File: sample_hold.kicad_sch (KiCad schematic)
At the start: 47 parts, among them K21 G6K-2FY, 5V, Q21 AO3400A, Q22 AO3401A, Q23 AO3400A, Q24 AO3400A, Q25 AO3400A, Q26 AO3400A, Q27 AO3400A, Q28 BSS139, Q29 BSS139, U21 OPA828DGN, U22 OPA2197D, U23 TLV9352D

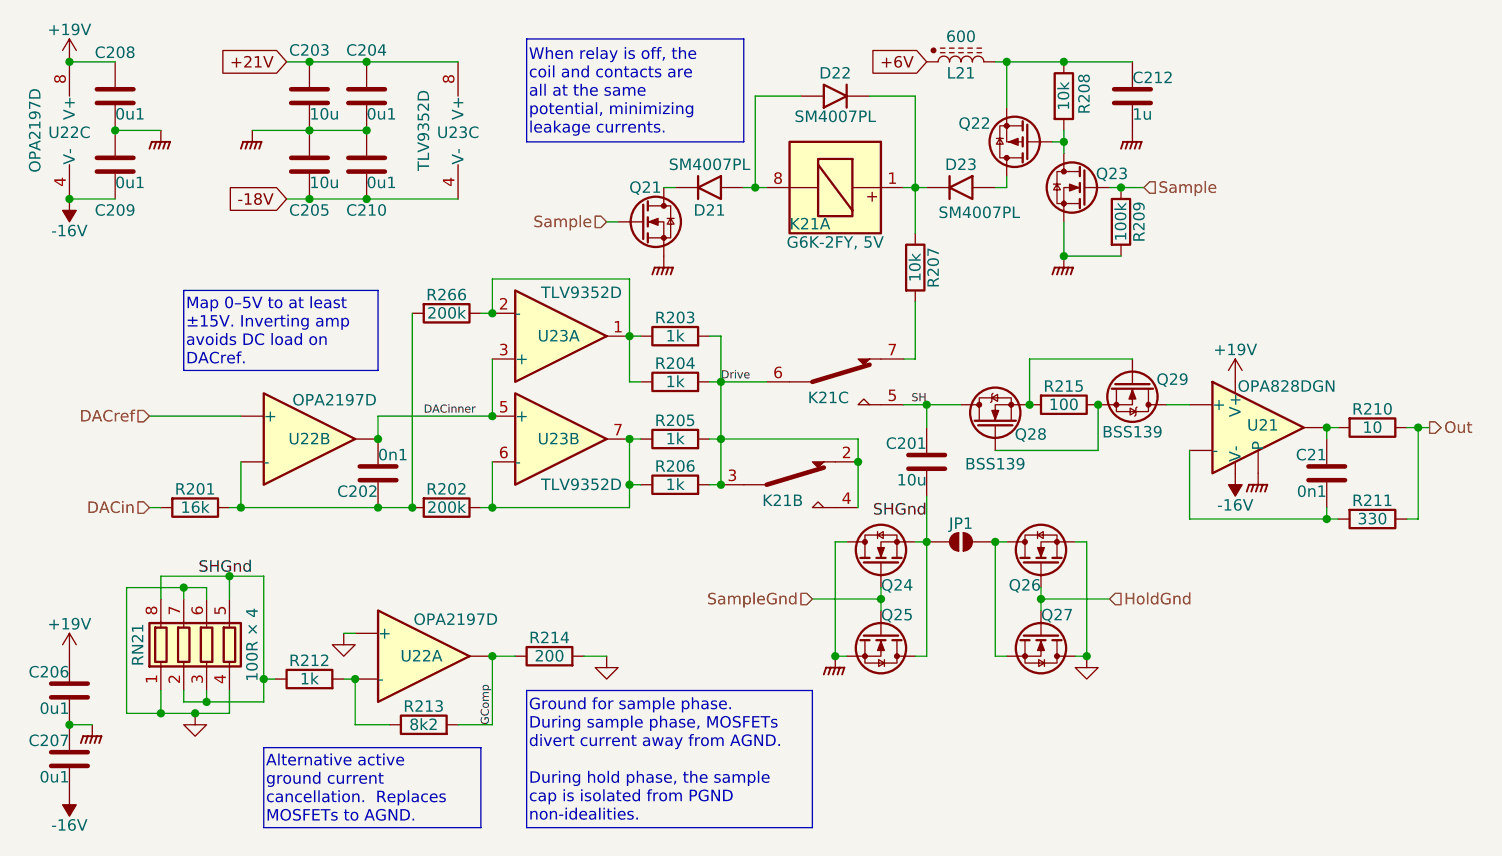
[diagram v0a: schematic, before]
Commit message: Nearly all routed.  Repinning FDA resistors.
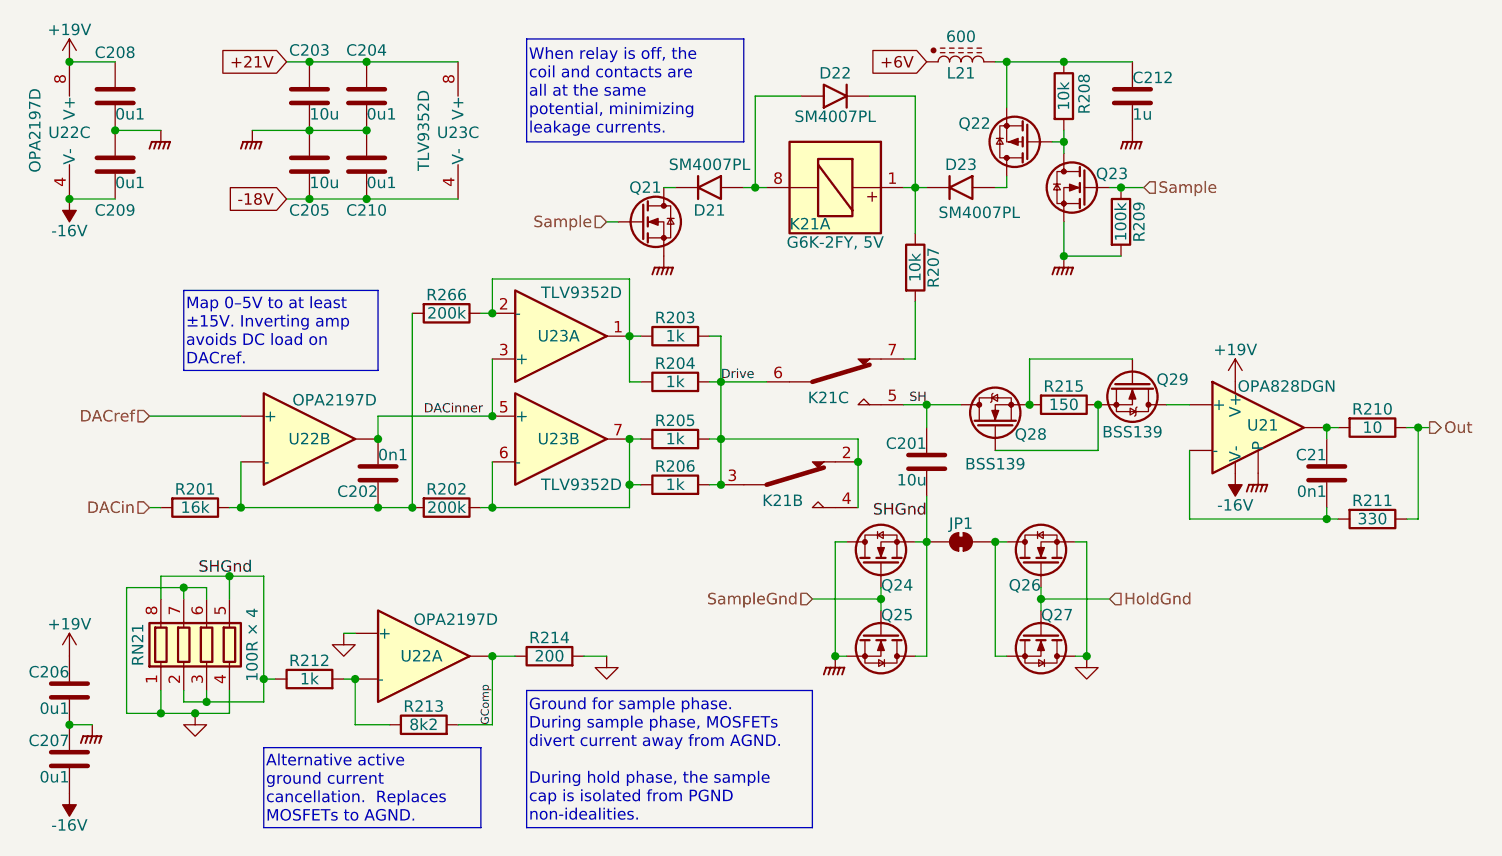
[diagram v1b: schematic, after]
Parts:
- C202, C21: footprint Capacitor_SMD:C_0402_1005Metric -> Capacitor_SMD:C_0603_1608Metric; LCSC C1546 -> (none)
- JP1: footprint Parts:JumperOpen -> Parts:JumperClosed; symbol Jumper:SolderJumper_2_Open -> Jumper:SolderJumper_2_Bridged
- R215: value 100 -> 150; LCSC (none) -> C25076
- U21: footprint Parts:OPA828DGN_guard -> Parts:OPA828DGN
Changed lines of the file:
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@@
 		(effects
 			(font
-				(size 0.889 0.889)
+				(size 1.016 1.016)
 			)
 			(justify left bottom)
@@
 			(font
 				(size 1.27 1.27)
+				(thickness 0.1588)
 			)
 			(justify right bottom)
@@
 		(effects
 			(font
-				(size 0.889 0.889)
+				(size 1.016 1.016)
 			)
 			(justify left bottom)
@@
 		(effects
 			(font
-				(size 0.889 0.889)
+				(size 1.016 1.016)
 			)
 			(justify right bottom)
@@
 			)
 		)
-		(property "Footprint" "Capacitor_SMD:C_0402_1005Metric"
+		(property "Footprint" "Capacitor_SMD:C_0603_1608Metric"
 			(at 106.3752 77.47 0)
 			(effects
@@
 			)
 		)
-		(property "LCSC" "C1546"
+		(property "LCSC" ""
 			(at 105.41 73.66 0)
 			(effects
@@
 			)
 		)
-		(property "Value" "100"
+		(property "Value" "150"
 			(at 181.61 66.04 90)
 			(effects
@@
 			)
 		)
-		(property "LCSC" ""
+		(property "LCSC" "C25076"
 			(at 181.61 66.04 90)
 			(effects
@@
 	)
 	(symbol
-		(lib_id "Jumper:SolderJumper_2_Open")
+		(lib_id "Jumper:SolderJumper_2_Bridged")
 		(at 170.18 81.28 0)
 		(unit 1)
@@
 			)
 		)
-		(property "Footprint" "Parts:JumperOpen"
+		(property "Footprint" "Parts:JumperClosed"
 			(at 170.18 81.28 0)
 			(effects
@@
 			)
 		)
-		(property "Description" "Solder Jumper, 2-pole, open"
+		(property "Description" "Solder Jumper, 2-pole, closed/bridged"
 			(at 170.18 81.28 0)
 			(effects
@@
 			)
 		)
-		(property "Footprint" "Parts:OPA828DGN_guard"
+		(property "Footprint" "Parts:OPA828DGN"
 			(at 200.66 73.66 0)
 			(effects
@@
 			)
 		)
-		(property "Footprint" "Capacitor_SMD:C_0402_1005Metric"
+		(property "Footprint" "Capacitor_SMD:C_0603_1608Metric"
 			(at 211.7852 77.47 0)
 			(effects
@@
 			)
 		)
-		(property "LCSC" "C1546"
+		(property "LCSC" ""
 			(at 210.82 73.66 0)
 			(effects

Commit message: DRC update.  Repin ADC.  De-crack the S/H ground.
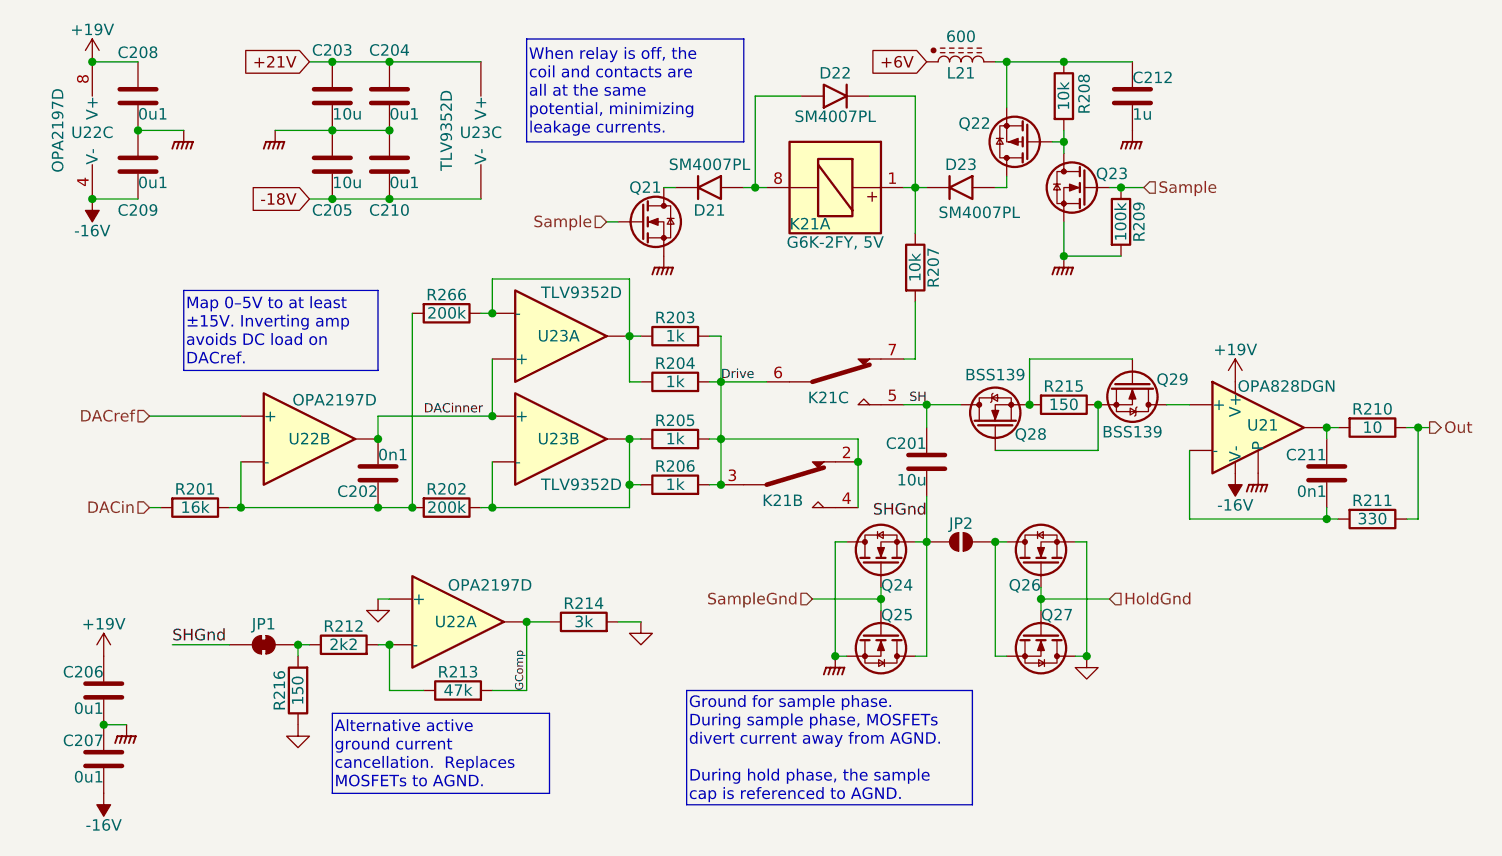
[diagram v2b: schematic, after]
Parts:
- removed RN21: 100R × 4, Resistor_SMD:R_Array_Convex_4x0603, symbol Device:R_Pack04
- added JP1: SolderJumper_2_Bridged, Parts:JumperClosed, symbol Jumper:SolderJumper_2_Bridged
- added R216: 150, Resistor_SMD:R_0402_1005Metric, symbol Device:R
- JP2: renamed from JP1; symbol Jumper:SolderJumper_2_Bridged -> Jumper:SolderJumper_2_Open
- R212: value 1k -> 2k2; footprint Resistor_SMD:R_0402_1005Metric -> Resistor_SMD:R_0603_1608Metric; LCSC C11702 -> (none)
- R213: value 8k2 -> 47k; LCSC C25981 -> (none)
- R214: value 200 -> 3k
- renumbered C21 to C211
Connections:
- net GND: now also R216.1
- net SHGnd: now also JP1.1 (A); no longer R212.1
- new net: JP1.2 (B), R212.1, R216.2
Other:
- moved on the sheet: C203, C204, C205, C206, C207, C208, C209, C210, R212, R213, R214, U22A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

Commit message: Rationalise and more SPI tidy.
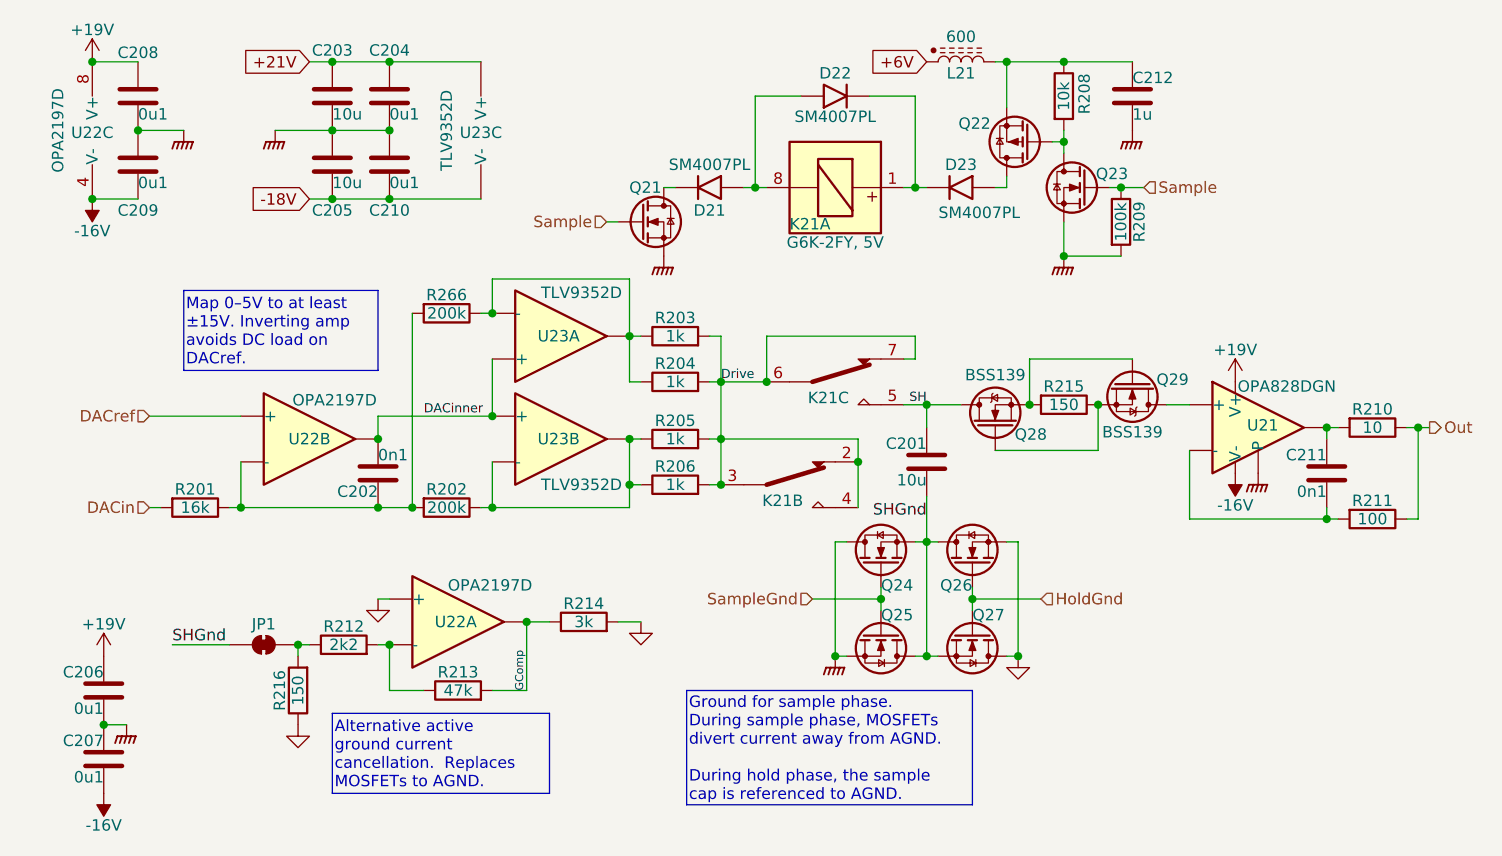
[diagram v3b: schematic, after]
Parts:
- removed JP2: SolderJumper_2_Open, Parts:JumperClosed, symbol Jumper:SolderJumper_2_Open
- removed R207: 10k, Resistor_SMD:R_0402_1005Metric, symbol Device:R
- R211: value 330 -> 100; LCSC C25104 -> C25076
- R216: LCSC (none) -> C25076
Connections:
- net Drive: now also K21.7
- net SHGnd: now also Q26.3 (D), Q27.2 (S)
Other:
- moved on the sheet: Q26, Q27

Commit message: Redo the reference ground star point.
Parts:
- added C213: 10u, Capacitor_SMD:C_0402_1005Metric, symbol Device:C
- added R207: 1, Resistor_SMD:R_0603_1608Metric, symbol Device:R
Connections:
- net GNDPWR: now also C213.2
- net GND renamed AGND
- net AGND: now also R207.1
- new net: C213.1, R207.2

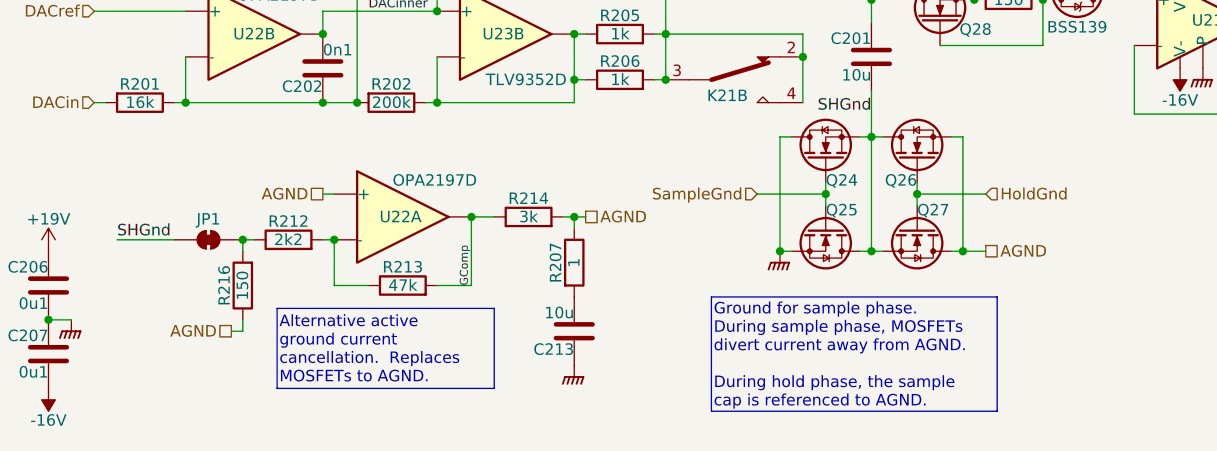
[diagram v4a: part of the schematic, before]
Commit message: Remove placebo planes.  Tidy some analog routing.
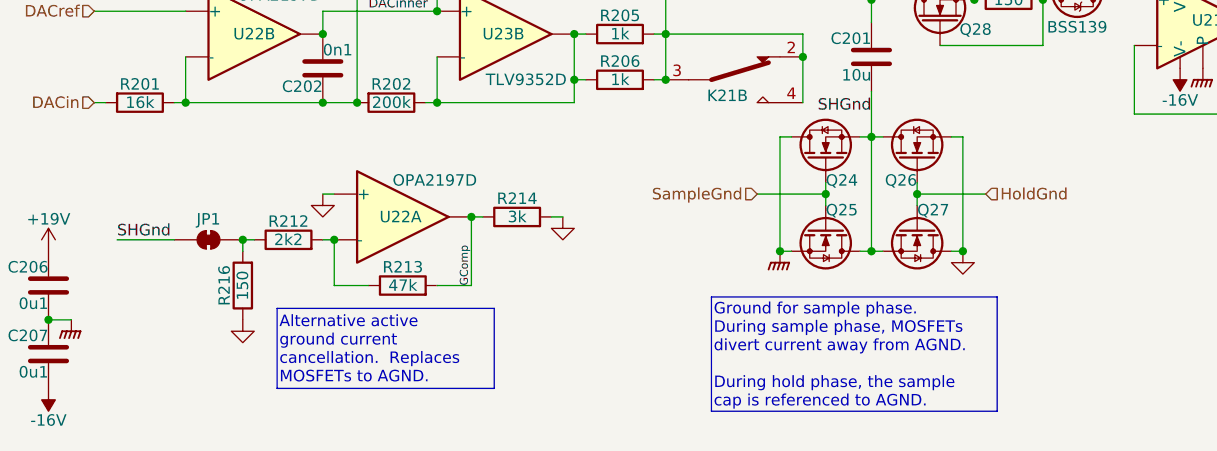
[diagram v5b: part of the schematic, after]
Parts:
- removed C213: 10u, Capacitor_SMD:C_0402_1005Metric, symbol Device:C
- removed R207: 1, Resistor_SMD:R_0603_1608Metric, symbol Device:R
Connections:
- net AGND renamed GND
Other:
- moved on the sheet: R214
